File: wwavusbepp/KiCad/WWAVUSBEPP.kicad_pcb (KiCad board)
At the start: 4 copper layers, 42.2 x 42.7 mm, 36 parts, among them J1 USB_B, J2 Conn_01x26_Female, J3 Conn_01x06_Female, J4 Conn_01x04_Male, U1 CY7C68013-56LFC, U2 LT1762-3.3, U3 NCP302LSN45T1G, U4 FM24C64B, Y1 24Mhz

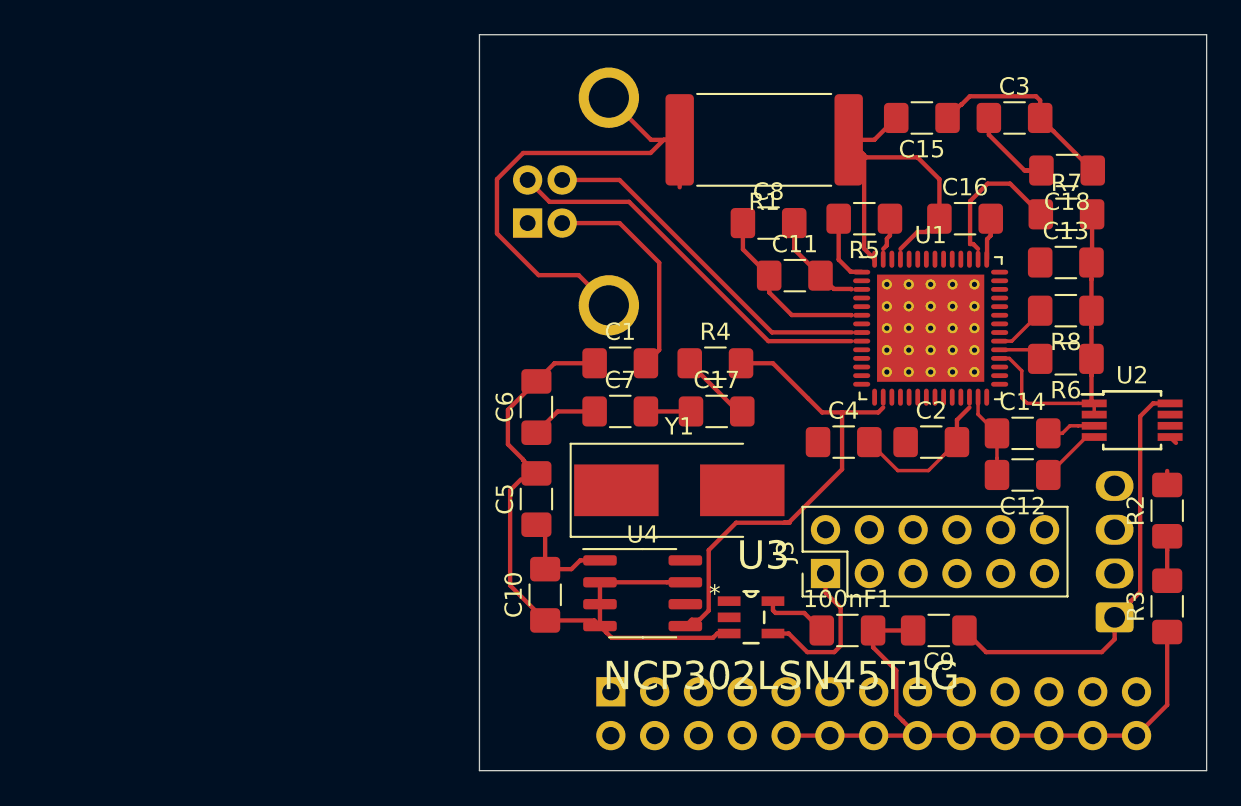
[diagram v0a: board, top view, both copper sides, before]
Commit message: Fixes to schematic and renaming components to match website image info.
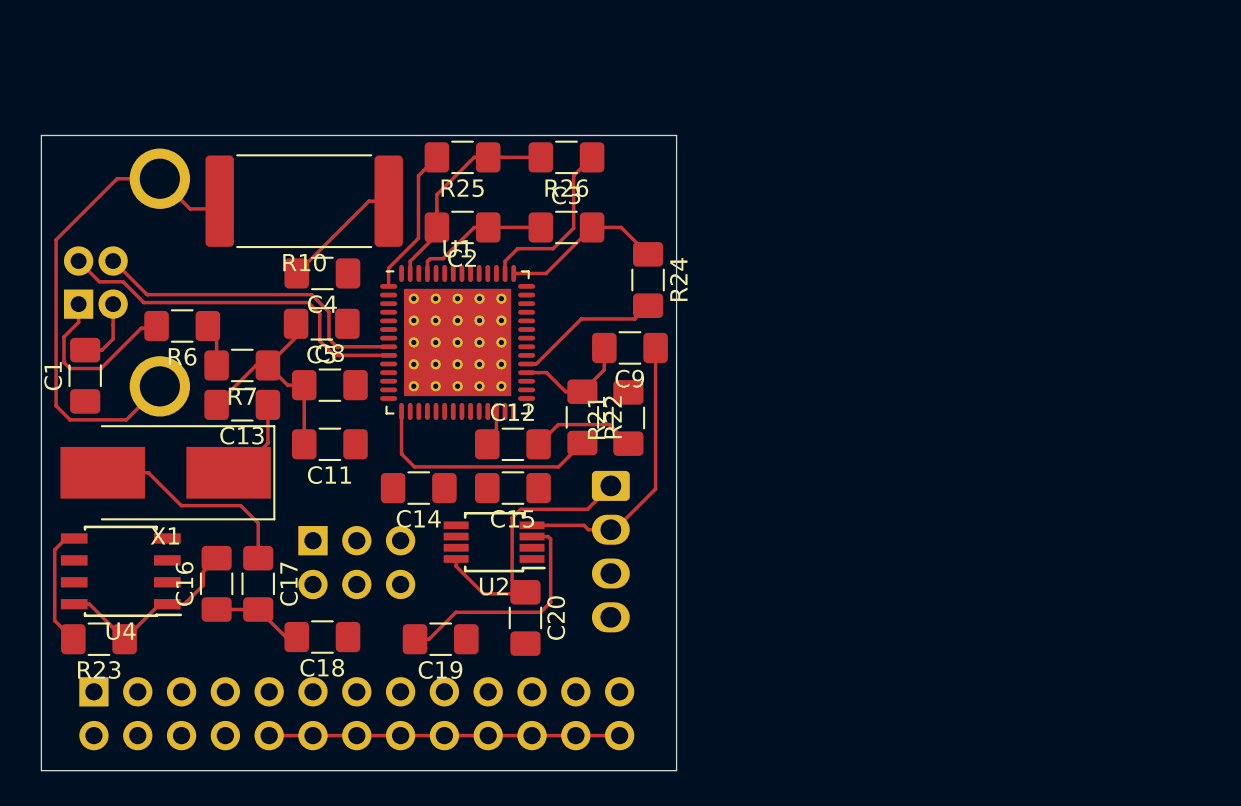
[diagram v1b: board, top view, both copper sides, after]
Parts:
- removed 100nF1, C10, C6, C7: 100nF, Capacitor_SMD:C_1206_3216Metric_Pad1.42x1.75mm_HandSolder
- removed R1: 1M, Resistor_SMD:R_4020_10251Metric_Pad1.65x5.30mm_HandSolder
- removed R2, R3: R_US, Resistor_SMD:R_1206_3216Metric_Pad1.42x1.75mm_HandSolder
- removed R4: 2.2k, Resistor_SMD:R_1206_3216Metric_Pad1.42x1.75mm_HandSolder
- removed R5, R8: 10k, Resistor_SMD:R_1206_3216Metric_Pad1.42x1.75mm_HandSolder
- removed U3: NCP302LSN45T1G, Package_SO:SOT95P275X110-5N
- removed Y1: 24Mhz, Crystal:Crystal_SMD_7050-2Pin_7.0x5.0mm_HandSoldering
- added C19: 100nF, Capacitor_SMD:C_1206_3216Metric_Pad1.42x1.75mm_HandSolder, F.Cu at (81.8, 148.6)
- added C20: 10uF, Capacitor_SMD:C_1206_3216Metric_Pad1.42x1.75mm_HandSolder, F.Cu at (86.7, 147.4)
- added R10: 1M, Resistor_SMD:R_4020_10251Metric_Pad1.65x5.30mm_HandSolder, F.Cu at (73.9, 123.2)
- added R21: 10k, Resistor_SMD:R_1206_3216Metric_Pad1.42x1.75mm_HandSolder, F.Cu at (92.7, 135.8)
- added R22: 10k, Resistor_SMD:R_1206_3216Metric_Pad1.42x1.75mm_HandSolder, F.Cu at (90.0, 135.7)
- added R23: 2.2k, Resistor_SMD:R_1206_3216Metric_Pad1.42x1.75mm_HandSolder, F.Cu at (62.0, 148.6)
- added R24: 2.2k, Resistor_SMD:R_1206_3216Metric_Pad1.42x1.75mm_HandSolder, F.Cu at (93.9, 127.8)
- added R25: 10k, Resistor_SMD:R_1206_3216Metric_Pad1.42x1.75mm_HandSolder, F.Cu at (83.1, 120.7)
- added R26: 10k, Resistor_SMD:R_1206_3216Metric_Pad1.42x1.75mm_HandSolder, F.Cu at (89.1, 120.7)
- added X1: 24Mhz, Crystal:Crystal_SMD_7050-2Pin_7.0x5.0mm_HandSoldering, F.Cu at (65.9, 138.9)
- C11: value 100nF -> 2.2uF
- C13: value 10nF -> 12pF
- C15: value 100nF -> 10uF
- C17: value 100nF -> 12pF
- C18: value 2.2uF -> 100nF
- C2, C4: value 12pF -> 100nF
- C9: value 10uF -> 100nF
- J3: footprint Connector_PinHeader_2.54mm:PinHeader_2x06_P2.54mm_Vertical -> Connector_PinHeader_2.54mm:PinHeader_2x03_P2.54mm_Vertical; moved to B.Cu
- R6: value 2.2k -> R_US
- R7: value 10k -> R_US
- moved R6 51.3 mm to (66.8, 130.4)
- moved C18 51.0 mm to (75.0, 148.5)
- moved R7 48.6 mm to (70.3, 132.7), turned to 180 degrees
- moved C13 48.5 mm to (70.3, 135.0), turned to 180 degrees
- moved C16 48.3 mm to (68.8, 145.4), turned to 90 degrees
- moved U2 37.7 mm to (84.9, 143.0), turned to 180 degrees
- moved C14 35.2 mm to (80.6, 139.8), turned to 180 degrees
- moved C15 32.0 mm to (86.0, 139.8)
- moved C4 31.8 mm to (75.0, 127.4), turned to 180 degrees
- moved C1 31.0 mm to (61.2, 133.3), turned to 90 degrees
- moved U4 30.3 mm to (63.3, 144.7), turned to 180 degrees
- moved J4 30.2 mm to (91.7, 139.7), turned to 270 degrees
- moved J2 30.0 mm to (61.7, 151.6)
- moved C2 29.9 mm to (83.1, 124.7), turned to 180 degrees
- moved J3 29.8 mm to (74.4, 142.9), turned to 270 degrees
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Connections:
- C11 pad 1: Earth -> +3V3
- C11 pad 2: +3V3 -> Earth
- C13 pad 1: Earth -> XTALIN
- C13 pad 2: +3V3 -> Earth
- C14 pad 1: +3V3 -> Earth
- C14 pad 2: Net-(C14-Pad2) -> +3V3
- C17 pad 1: Earth -> XTALOUT
- C17 pad 2: +3V3 -> Earth
- C18 pad 1: +3V3 -> Net-(C18-Pad1)
- C2 pad 1: XTALIN -> Earth
- C2 pad 2: Earth -> +3V3
- C4 pad 1: XTALOUT -> +3V3
- C9 pad 1: Net-(C9-Pad1) -> Earth
- C9 pad 2: Earth -> +3V3
- J3 pad 1: (no net) -> Net-(J3-Pad1)
- J3 pad 2: (no net) -> Net-(J3-Pad2)
- J3 pad 3: (no net) -> Net-(J3-Pad3)
- J3 pad 4: (no net) -> Net-(J3-Pad4)
- J3 pad 5: (no net) -> Net-(J3-Pad5)
- J3 pad 6: (no net) -> Net-(J3-Pad6)
- J4 pad 1: Net-(C9-Pad1) -> Net-(C20-Pad1)
- J4 pad 3: (no net) -> Net-(J4-Pad3)
- J4 pad 4: (no net) -> Net-(J4-Pad4)
- R6 pad 1: +3V3 -> Net-(R6-Pad1)
- R6 pad 2: Net-(J2-Pad19) -> Net-(J1-Pad1)
- R7 pad 1: Net-(R7-Pad1) -> Earth
- R7 pad 2: +3V3 -> Net-(R6-Pad1)
- U1 pad 13: (no net) -> Net-(U1-Pad13)
- U1 pad 36: (no net) -> Net-(U1-Pad36)
- U1 pad 37: (no net) -> Net-(U1-Pad37)
- U1 pad 39: (no net) -> Net-(U1-Pad39)
- U1 pad 40: (no net) -> Net-(U1-Pad40)
- U1 pad 44: Net-(R7-Pad1) -> Net-(R26-Pad1)
- U1 pad 45: (no net) -> Net-(U1-Pad45)
- U1 pad 46: (no net) -> Net-(U1-Pad46)
- U1 pad 47: (no net) -> Net-(U1-Pad47)
- U1 pad 48: (no net) -> Net-(U1-Pad48)
- U1 pad 49: (no net) -> Net-(U1-Pad49)
- U1 pad 50: (no net) -> Net-(U1-Pad50)
- U1 pad 51: (no net) -> Net-(U1-Pad51)
- U1 pad 52: (no net) -> Net-(U1-Pad52)
- U1 pad 54: (no net) -> Net-(U1-Pad54)
- U2 pad 3: Net-(C14-Pad2) -> Net-(C19-Pad2)
- U2 pad 5: Net-(R2-Pad1) -> Net-(R6-Pad1)
- U2 pad 6: (no net) -> Net-(U2-Pad6)
- U2 pad 7: (no net) -> Net-(U2-Pad7)
- U2 pad 8: Net-(C9-Pad1) -> Net-(C20-Pad1)
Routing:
- net Earth: track 127.8 -> 72.4 mm
- net Net-(C9-Pad1): track 25.1 -> 0.00 mm
- net SDA: track 28.1 -> 7.03 mm
- net Net-(C20-Pad1): track 0.00 -> 16.3 mm
- net +3V3: track 60.9 -> 46.1 mm
- net SCL: track 0.00 -> 13.8 mm
- net Net-(C19-Pad2): track 0.00 -> 13.6 mm
- net XTALOUT: track 0.00 -> 12.3 mm
- net Net-(R26-Pad1): track 0.00 -> 10.0 mm
- net Net-(J1-Pad1): track 0.81 -> 10.1 mm
- net (no net): track 9.30 -> 0.00 mm
- net Net-(C1-Pad2): track 12.7 -> 3.91 mm
- net Net-(R7-Pad1): track 8.32 -> 0.00 mm
- net Net-(J2-Pad19): track 2.57 -> 8.45 mm
- net XTALIN: track 0.00 -> 5.22 mm
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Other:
- board size 42.2 x 42.7 mm -> 36.8 x 36.8 mm

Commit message: Fixed one footprint, and restarted traces.
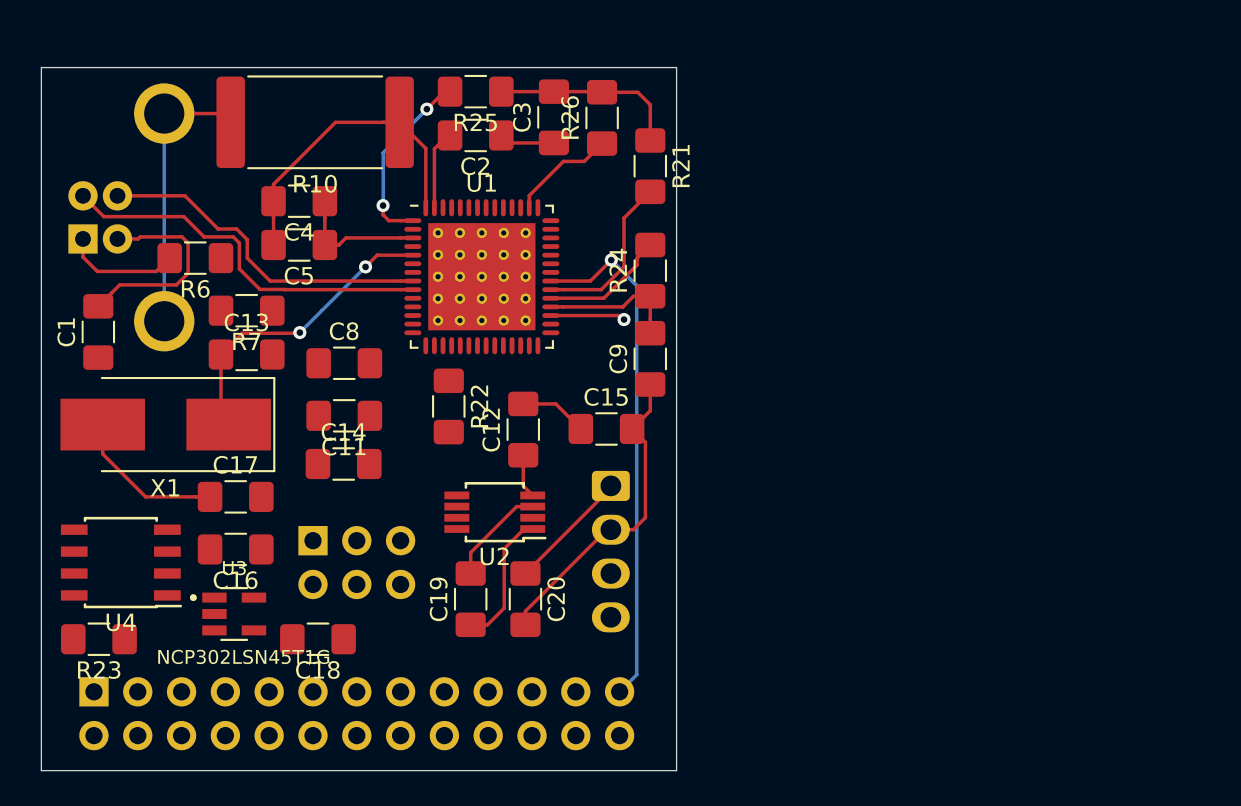
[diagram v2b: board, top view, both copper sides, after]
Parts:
- added U3: NCP302LSN45T1G, SOP95P275X110-5N:SOP95P275X110-5N, F.Cu at (69.9, 147.1)
- moved R21 14.7 mm to (94.0, 121.2), turned to 270 degrees
- moved R22 7.77 mm to (82.3, 135.1)
- moved C3 6.43 mm to (88.4, 118.3), turned to 90 degrees
- moved C15 6.42 mm to (91.4, 136.4), turned to 0 degrees
- moved C2 5.39 mm to (83.9, 119.4)
- moved C17 5.21 mm to (69.9, 140.3), turned to 0 degrees
- moved C5 4.76 mm to (73.6, 125.7)
- moved R10 4.62 mm to (74.5, 118.6)
- moved C14 4.57 mm to (76.2, 138.4), turned to 0 degrees
- moved C4 4.40 mm to (73.6, 123.2)
- moved U1 4.06 mm to (84.2, 127.6)
- moved R6 4.01 mm to (67.6, 126.5)
- moved R25 3.89 mm to (83.9, 116.8)
- moved J1 3.79 mm to (61.1, 125.4)
- moved R7 3.19 mm to (70.6, 129.5)
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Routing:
- net Earth: track 72.4 -> 42.1 mm
- net 25: track 0.00 -> 30.1 mm, vias 0 -> 1
- net SCL: track 13.8 -> 0.00 mm
- net Net-(J1-Pad5): track 28.6 -> 16.1 mm
- net XTALIN: track 5.22 -> 17.8 mm, vias 0 -> 2
- net Net-(J2-Pad4): track 0.00 -> 9.78 mm
- net Net-(C20-Pad1): track 16.3 -> 7.13 mm
- net Net-(C1-Pad2): track 3.91 -> 12.0 mm
- net Net-(C19-Pad2): track 13.6 -> 5.91 mm
- net SDA: track 7.03 -> 0.00 mm
- net 8: track 0.00 -> 4.34 mm, vias 0 -> 1
- net Net-(R26-Pad1): track 10.0 -> 6.18 mm
- net Net-(J1-Pad1): track 10.1 -> 6.74 mm
- net XTALOUT: track 12.3 -> 8.96 mm
- net +3V3: track 46.1 -> 43.4 mm
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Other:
- board size 36.8 x 36.8 mm -> 36.8 x 40.8 mm

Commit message: Updates to routes, not complete.
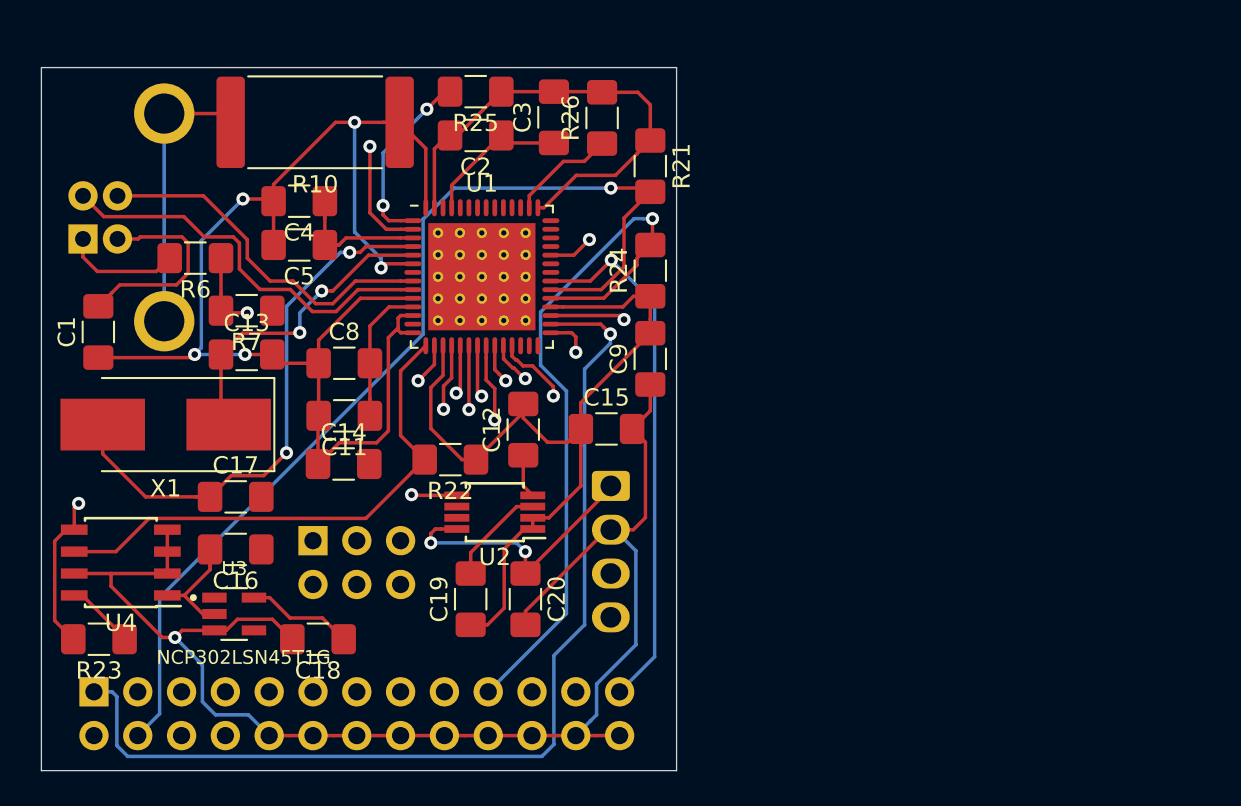
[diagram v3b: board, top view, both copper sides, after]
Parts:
- moved R22 3.09 mm to (82.4, 138.2), turned to 180 degrees
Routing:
- net Earth: track 42.1 -> 175.7 mm, vias 0 -> 6
- net +3V3: track 43.4 -> 102.8 mm
- net 1: track 0.00 -> 59.0 mm, vias 0 -> 1
- net 6: track 0.00 -> 51.4 mm, vias 0 -> 1
- net Net-(J2-Pad4): track 9.78 -> 60.6 mm, vias 0 -> 1
- net 23: track 0.00 -> 49.6 mm, vias 0 -> 1
- net 2: track 0.00 -> 49.2 mm, vias 0 -> 1
- net 8: track 4.34 -> 51.8 mm
- net Net-(J2-Pad21): track 10.8 -> 49.8 mm
- net 3: track 0.00 -> 34.9 mm, vias 0 -> 1
- net Net-(J2-Pad19): track 7.28 -> 42.1 mm, vias 0 -> 1
- net SDA: track 0.00 -> 34.2 mm, vias 0 -> 2
- net 5: track 0.00 -> 33.4 mm, vias 0 -> 1
- net 7: track 0.00 -> 31.7 mm, vias 0 -> 1
- net SCL: track 0.00 -> 30.3 mm
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
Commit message: Completed traces, not silk.
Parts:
- moved C12 1.74 mm to (86.6, 138.2), turned to 180 degrees
- moved R22 0.89 mm to (81.5, 138.2)
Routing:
- net +3V3: track 102.8 -> 200.4 mm, vias 0 -> 9
- net Earth: track 175.7 -> 267.4 mm, vias 6 -> 18
- net U3_R: track 0.00 -> 51.4 mm, vias 0 -> 2
- net 3: track 34.9 -> 36.2 mm
- net XTALIN: track 18.4 -> 19.7 mm
- net XTALOUT: track 31.7 -> 32.7 mm
- net 15: track 25.6 -> 24.6 mm
- net 17: track 24.4 -> 25.4 mm
- net 5: track 33.4 -> 34.3 mm
- net Net-(J2-Pad21): track 49.8 -> 49.2 mm
- net 7: track 31.7 -> 32.2 mm
- net 13: track 26.8 -> 26.3 mm
